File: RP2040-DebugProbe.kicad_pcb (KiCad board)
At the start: 4 copper layers, 50.8 x 25.4 mm, 60 parts, among them J1 CONN_MCU_JTAG, J10 CONN_USB, J2 CONN_MCU_UART, J3 CONN_DBG_COMB, J4 CONN_3V3_JUMPER, J7 CONN_DBG_JTAG, SW1 BOOTSEL, U1 W25Q128JVS, U2 RP2040, U3 74AUP1T17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

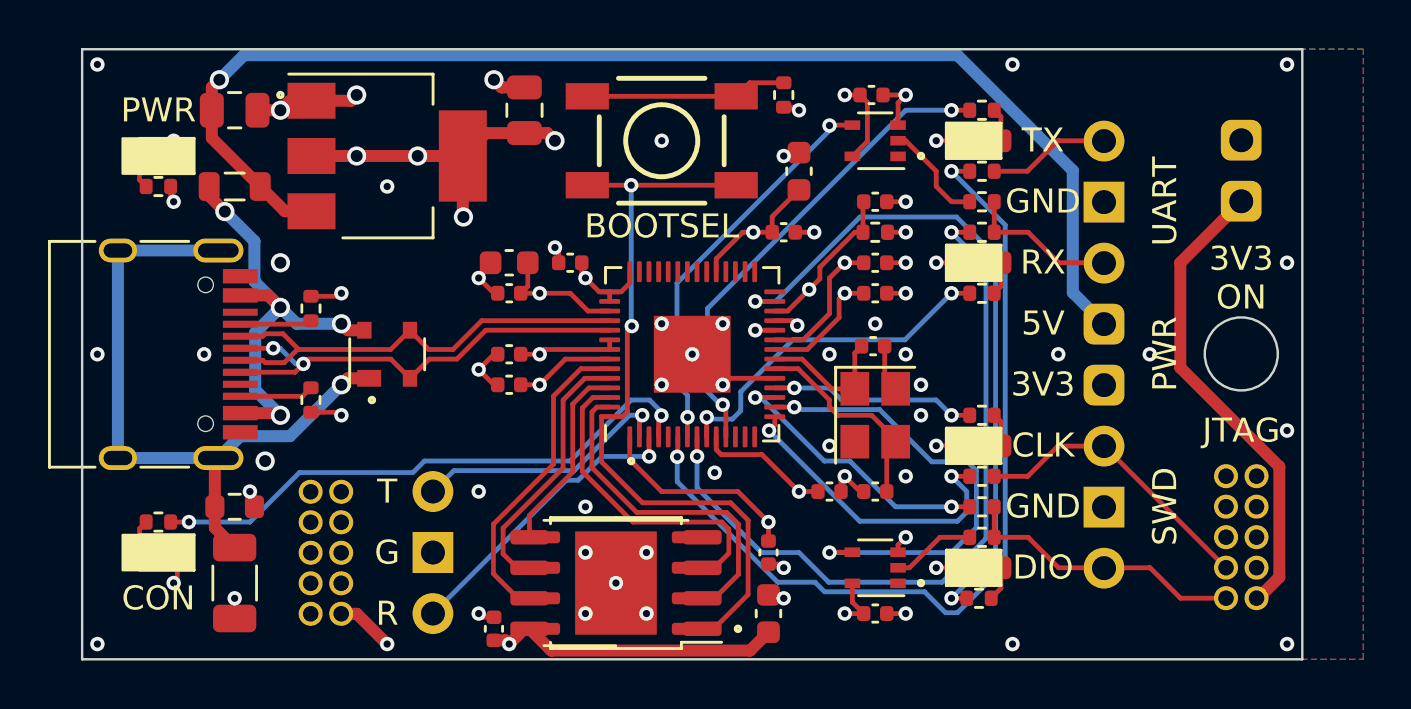
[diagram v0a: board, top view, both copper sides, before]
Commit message: Added target reset line on GPIO 10
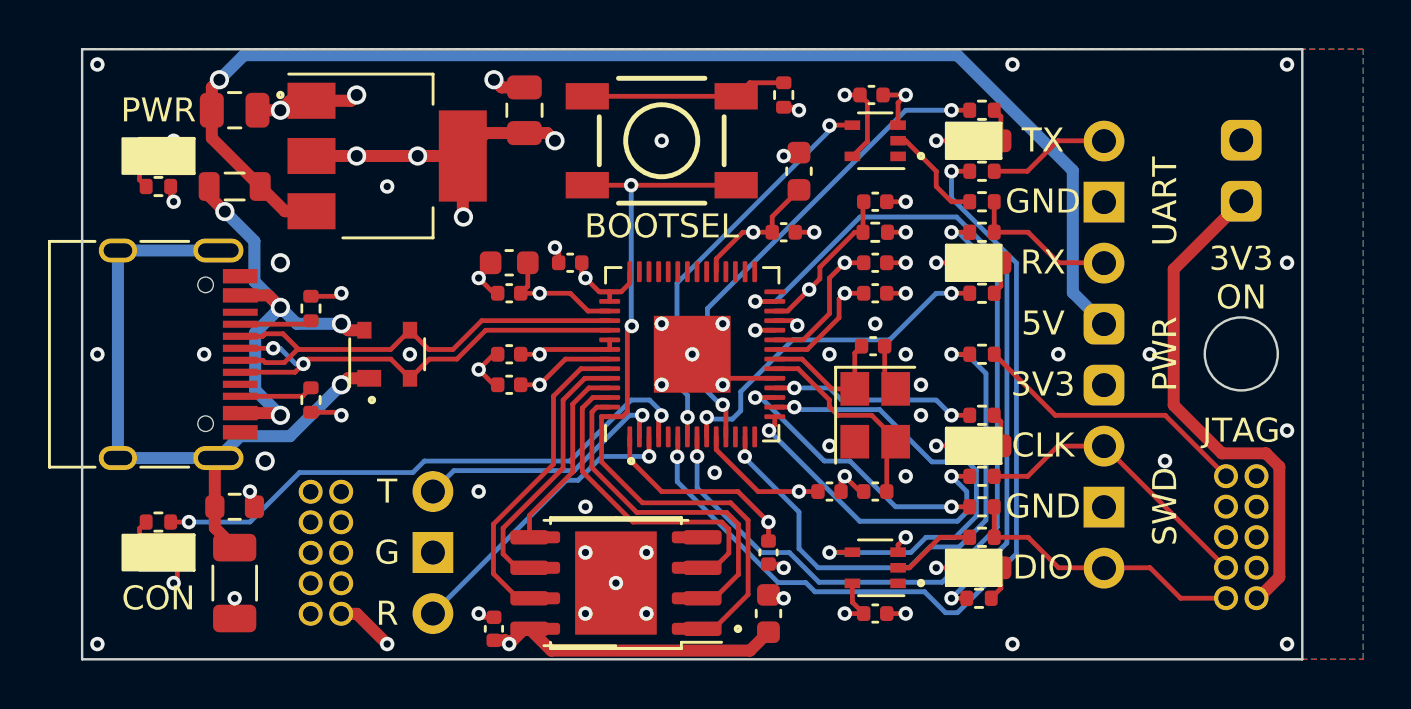
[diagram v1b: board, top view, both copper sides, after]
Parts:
- added R18: 100R, Resistor_SMD:R_0402_1005Metric, F.Cu at (164.5, 108.0)
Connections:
- J7 pad 10: unconnected-(J7-~{RESET}-Pad10) -> TARGET_RESET
- U2 pad 13: unconnected-(U2-GPIO10-Pad13) -> DBG_RESET
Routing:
- net DBG_RESET: track 0.00 -> 23.2 mm, vias 0 -> 2
- net TARGET_RESET: track 0.00 -> 11.8 mm
- net TARGET_3V3: track 19.7 -> 21.0 mm
- net UART_RX: track 30.6 -> 31.2 mm
- net GND: vias 65 -> 67

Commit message: Added host side protection resistors
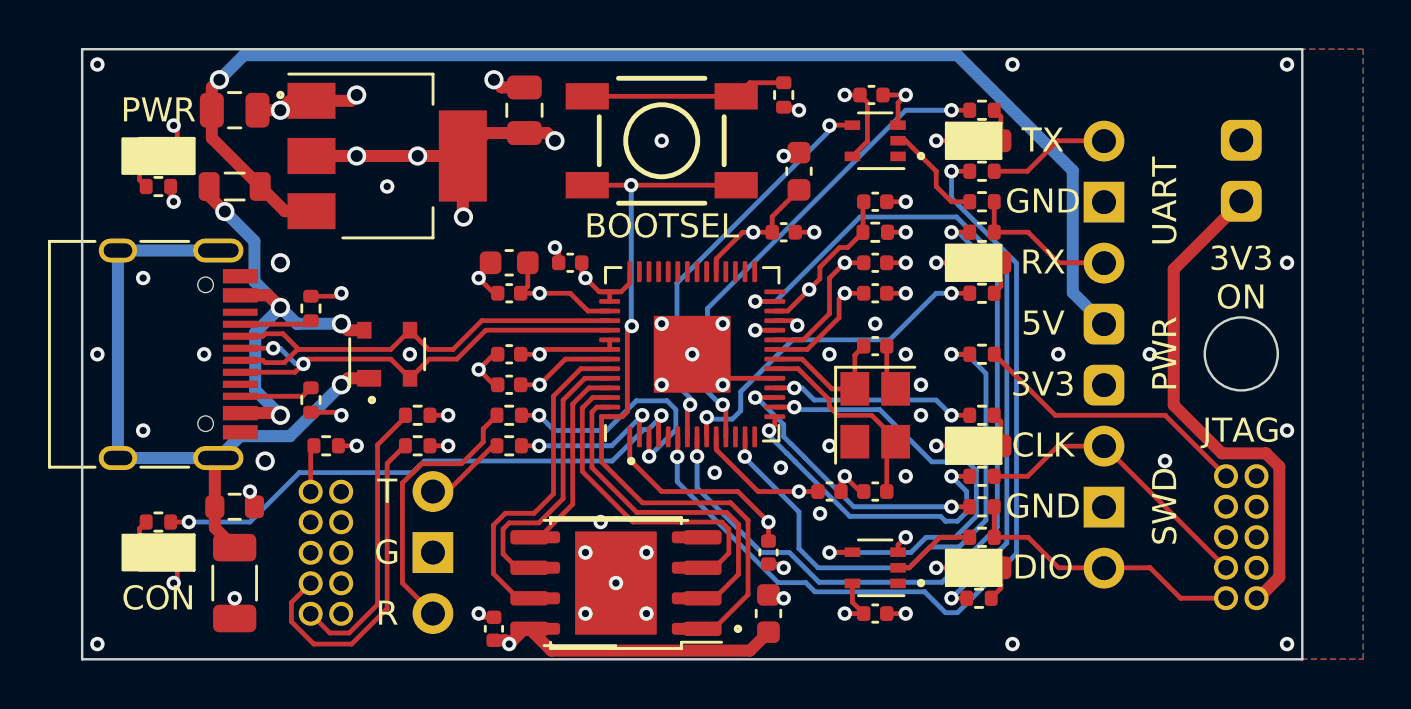
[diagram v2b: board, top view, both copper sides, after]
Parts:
- added R19: 100R, Resistor_SMD:R_0402_1005Metric, F.Cu at (144.8, 111.8)
- added R20: 100R, Resistor_SMD:R_0402_1005Metric, F.Cu at (144.8, 110.5)
- added R21: 100R, Resistor_SMD:R_0402_1005Metric, F.Cu at (137.2, 111.8)
- added R22: 100R, Resistor_SMD:R_0402_1005Metric, F.Cu at (141.0, 111.8)
- added R23: 100R, Resistor_SMD:R_0402_1005Metric, F.Cu at (141.0, 110.5)
- moved C20 0.09 mm to (160.0, 107.6)
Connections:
- J1 pad 10: MCU_RESET -> HOST_RESET
- J1 pad 2: MCU_DIO -> HOST_DIO
- J1 pad 4: MCU_CLK -> HOST_CLK
- J2 pad 1: MCU_TX -> HOST_TX
- J2 pad 3: MCU_RX -> HOST_RX
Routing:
- net MCU_CLK: track 37.2 -> 22.5 mm, vias 1 -> 2
- net HOST_CLK: track 0.00 -> 14.0 mm
- net MCU_DIO: track 30.7 -> 18.6 mm, vias 1 -> 2
- net HOST_DIO: track 0.00 -> 12.0 mm
- net HOST_RX: track 0.00 -> 11.4 mm
- net MCU_TX: track 11.0 -> 6.51 mm, vias 1 -> 2
- net HOST_TX: track 0.00 -> 3.45 mm
- net +3V3: track 68.9 -> 66.4 mm, vias 16 -> 15
- net HOST_RESET: track 0.00 -> 1.97 mm
- net MCU_RESET: track 30.9 -> 29.0 mm, vias 1 -> 2
- net MCU_RX: track 12.5 -> 10.6 mm, vias 1 -> 2
- net QSPI_SCLK: track 11.1 -> 11.8 mm
- net QSPI_SD3: track 13.2 -> 13.9 mm
- net LED_ACT: track 23.8 -> 23.2 mm
- net GND: track 37.7 -> 38.3 mm, vias 67 -> 70

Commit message: Moved stuff around
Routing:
- net QSPI_SCLK: track 11.8 -> 11.1 mm
- net QSPI_SD3: track 13.9 -> 13.2 mm
- net GND: vias 70 -> 73
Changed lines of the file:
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@@
   (via (at 149.225 117.475) (size 0.6) (drill 0.3) (layers "F.Cu" "B.Cu") (net 2))
   (via (at 161.925 109.22) (size 0.6) (drill 0.3) (layers "F.Cu" "B.Cu") (free) (net 2))
-  (via (at 148.59 114.935) (size 0.6) (drill 0.3) (layers "F.Cu" "B.Cu") (free) (net 2))
+  (via (at 147.32 114.3) (size 0.6) (drill 0.3) (layers "F.Cu" "B.Cu") (free) (net 2))
   (via (at 158.75 113.03) (size 0.6) (drill 0.3) (layers "F.Cu" "B.Cu") (free) (net 2))
   (via (at 147.955 118.745) (size 0.6) (drill 0.3) (layers "F.Cu" "B.Cu") (net 2))
@@
   (via (at 161.925 110.49) (size 0.6) (drill 0.3) (layers "F.Cu" "B.Cu") (free) (net 2))
   (via (at 144.145 96.52) (size 0.8) (drill 0.5) (layers "F.Cu" "B.Cu") (net 2))
+  (via (at 173.355 116.84) (size 0.6) (drill 0.3) (layers "F.Cu" "B.Cu") (free) (net 2))
   (via (at 150.495 118.745) (size 0.6) (drill 0.3) (layers "F.Cu" "B.Cu") (net 2))
   (via (at 156.090188 112.670566) (size 0.6) (drill 0.3) (layers "F.Cu" "B.Cu") (free) (net 2))
@@
   (via (at 156.21 99.695) (size 0.6) (drill 0.3) (layers "F.Cu" "B.Cu") (net 2))
   (via (at 153.333822 112.880587) (size 0.6) (drill 0.3) (layers "F.Cu" "B.Cu") (free) (net 2))
+  (via (at 139.7 120.015) (size 0.6) (drill 0.3) (layers "F.Cu" "B.Cu") (free) (net 2))
   (via (at 129.54 104.775) (size 0.6) (drill 0.3) (layers "F.Cu" "B.Cu") (free) (net 2))
   (via (at 127.635 120.015) (size 0.6) (drill 0.3) (layers "F.Cu" "B.Cu") (free) (net 2))
@@
   (via (at 151.13 106.68) (size 0.6) (drill 0.3) (layers "F.Cu" "B.Cu") (net 2))
   (via (at 172.085 112.395) (size 0.6) (drill 0.3) (layers "F.Cu" "B.Cu") (free) (net 2))
+  (via (at 144.78 113.03) (size 0.6) (drill 0.3) (layers "F.Cu" "B.Cu") (free) (net 2))
   (via (at 162.56 104.14) (size 0.6) (drill 0.3) (layers "F.Cu" "B.Cu") (net 2))
   (via (at 147.955 116.205) (size 0.6) (drill 0.3) (layers "F.Cu" "B.Cu") (net 2))
@@
   (segment (start 148.262954 109.75) (end 147.825 110.187954) (width 0.2) (layer "F.Cu") (net 52))
   (segment (start 153.630552 114.935) (end 153.925 115.229448) (width 0.2) (layer "F.Cu") (net 52))
+  (segment (start 148.9625 109.35) (end 148.097269 109.35) (width 0.2) (layer "F.Cu") (net 53))
+  (segment (start 145.625 114.695134) (end 145.625 115.57) (width 0.2) (layer "F.Cu") (net 53))
   (segment (start 148.097269 109.35) (end 147.425 110.022268) (width 0.2) (layer "F.Cu") (net 53))
-  (segment (start 146.05 115.57) (end 145.625 115.57) (width 0.2) (layer "F.Cu") (net 53))
-  (segment (start 147.425 110.022268) (end 147.425 114.195) (width 0.2) (layer "F.Cu") (net 53))
-  (segment (start 148.9625 109.35) (end 148.097269 109.35) (width 0.2) (layer "F.Cu") (net 53))
-  (segment (start 147.425 114.195) (end 146.05 115.57) (width 0.2) (layer "F.Cu") (net 53))
+  (segment (start 147.425 112.895134) (end 145.625 114.695134) (width 0.2) (layer "F.Cu") (net 53))
+  (segment (start 147.425 110.022268) (end 147.425 112.895134) (width 0.2) (layer "F.Cu") (net 53))
+  (segment (start 144.525 115.229448) (end 144.525 116.260854) (width 0.2) (layer "F.Cu") (net 54))
+  (segment (start 147.025 112.729448) (end 144.525 115.229448) (width 0.2) (layer "F.Cu") (net 54))
+  (segment (start 145.104146 116.84) (end 145.625 116.84) (width 0.2) (layer "F.Cu") (net 54))
+  (segment (start 147.025 109.856582) (end 147.025 112.729448) (width 0.2) (layer "F.Cu") (net 54))
+  (segment (start 148.9625 108.95) (end 147.931583 108.95) (width 0.2) (layer "F.Cu") (net 54))
+  (segment (start 147.931583 108.95) (end 147.025 109.856582) (width 0.2) (layer "F.Cu") (net 54))
   (segment (start 144.525 116.260854) (end 145.104146 116.84) (width 0.2) (layer "F.Cu") (net 54))
-  (segment (start 147.931583 108.95) (end 147.025 109.856582) (width 0.2) (layer "F.Cu") (net 54))
-  (segment (start 147.025 109.856582) (end 147.025 113.96) (width 0.2) (layer "F.Cu") (net 54))
-  (segment (start 144.784448 114.97) (end 144.525 115.229448) (width 0.2) (layer "F.Cu") (net 54))
-  (segment (start 145.104146 116.84) (end 145.625 116.84) (width 0.2) (layer "F.Cu") (net 54))
-  (segment (start 146.015 114.97) (end 144.784448 114.97) (width 0.2) (layer "F.Cu") (net 54))
-  (segment (start 147.025 113.96) (end 146.015 114.97) (width 0.2) (layer "F.Cu") (net 54))
-  (segment (start 144.525 115.229448) (end 144.525 116.260854) (width 0.2) (layer "F.Cu") (net 54))
-  (segment (start 148.9625 108.95) (end 147.931583 108.95) (width 0.2) (layer "F.Cu") (net 54))
-  (segment (start 144.125 115.063763) (end 144.125 117.087637) (width 0.2) (layer "F.Cu") (net 55))
-  (segment (start 145.814657 114.57) (end 144.618762 114.57) (width 0.2) (layer "F.Cu") (net 55))
-  (segment (start 147.765898 108.55) (end 146.625 109.690896) (width 0.2) (layer "F.Cu") (net 55))
-  (segment (start 145.147363 118.11) (end 145.625 118.11) (width 0.2) (layer "F.Cu") (net 55))
-  (segment (start 146.625 113.759657) (end 145.814657 114.57) (width 0.2) (layer "F.Cu") (net 55))
-  (segment (start 144.618762 114.57) (end 144.125 115.063763) (width 0.2) (layer "F.Cu") (net 55))
   (segment (start 144.125 117.087637) (end 145.147363 118.11) (width 0.2) (layer "F.Cu") (net 55))
   (segment (start 148.9625 108.55) (end 147.765898 108.55) (width 0.2) (layer "F.Cu") (net 55))
-  (segment (start 146.625 109.690896) (end 146.625 113.759657) (width 0.2) (layer "F.Cu") (net 55))
+  (segment (start 145.147363 118.11) (end 145.625 118.11) (width 0.2) (layer "F.Cu") (net 55))
+  (segment (start 146.625 112.563762) (end 144.125 115.063763) (width 0.2) (layer "F.Cu") (net 55))
+  (segment (start 147.765898 108.55) (end 146.625 109.690896) (width 0.2) (layer "F.Cu") (net 55))
+  (segment (start 146.625 109.690896) (end 146.625 112.563762) (width 0.2) (layer "F.Cu") (net 55))
+  (segment (start 144.125 115.063763) (end 144.125 117.087637) (width 0.2) (layer "F.Cu") (net 55))
   (segment (start 152.313214 110.049502) (end 152.2 110.162716) (width 0.2) (layer "F.Cu") (net 57))
   (segment (start 158.13 98.41) (end 158.115 98.425) (width 0.2) (layer "F.Cu") (net 57))

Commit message: Moved stuff around
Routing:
- net GND: vias 73 -> 76
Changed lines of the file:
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@@
   (via (at 167.64 107.95) (size 0.6) (drill 0.3) (layers "F.Cu" "B.Cu") (free) (net 2))
   (via (at 157.721926 114.580634) (size 0.6) (drill 0.3) (layers "F.Cu" "B.Cu") (free) (net 2))
+  (via (at 173.355 107.95) (size 0.6) (drill 0.3) (layers "F.Cu" "B.Cu") (free) (net 2))
   (via (at 135.255 104.14) (size 0.8) (drill 0.5) (layers "F.Cu" "B.Cu") (free) (net 2))
   (via (at 149.225 117.475) (size 0.6) (drill 0.3) (layers "F.Cu" "B.Cu") (net 2))
@@
   (via (at 153.67 109.22) (size 0.6) (drill 0.3) (layers "F.Cu" "B.Cu") (net 2))
   (via (at 171.45 107.95) (size 0.6) (drill 0.3) (layers "F.Cu" "B.Cu") (free) (net 2))
+  (via (at 166.37 101.6) (size 0.6) (drill 0.3) (layers "F.Cu" "B.Cu") (free) (net 2))
   (via (at 161.29 118.745) (size 0.6) (drill 0.3) (layers "F.Cu" "B.Cu") (net 2))
   (via (at 143.51 104.775) (size 0.6) (drill 0.3) (layers "F.Cu" "B.Cu") (net 2))
@@
   (via (at 173.355 116.84) (size 0.6) (drill 0.3) (layers "F.Cu" "B.Cu") (free) (net 2))
   (via (at 150.495 118.745) (size 0.6) (drill 0.3) (layers "F.Cu" "B.Cu") (net 2))
+  (via (at 167.005 111.125) (size 0.6) (drill 0.3) (layers "F.Cu" "B.Cu") (free) (net 2))
   (via (at 156.090188 112.670566) (size 0.6) (drill 0.3) (layers "F.Cu" "B.Cu") (free) (net 2))
   (via (at 130.81 98.425) (size 0.6) (drill 0.3) (layers "F.Cu" "B.Cu") (net 2))
